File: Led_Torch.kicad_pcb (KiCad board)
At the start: 2 copper layers, 63.8 x 25 mm, 5 parts, among them SW1 SW_DPST_x2

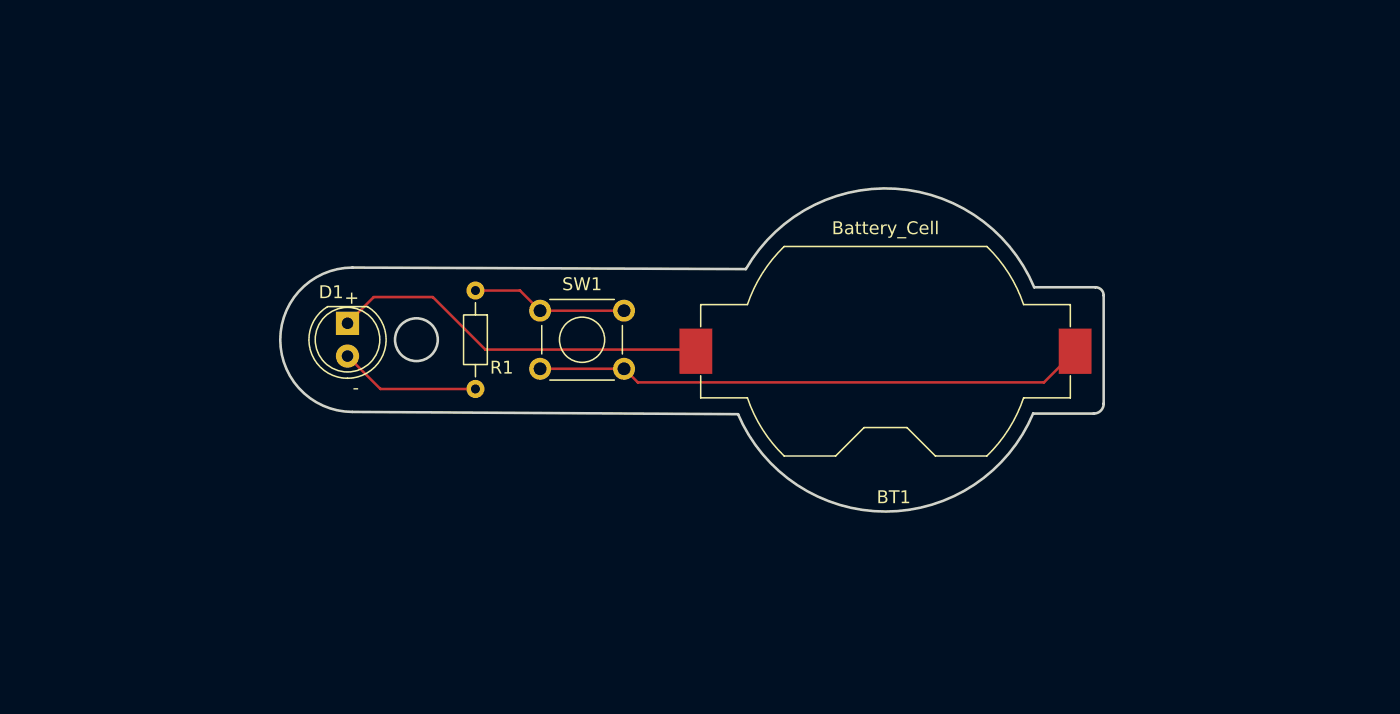
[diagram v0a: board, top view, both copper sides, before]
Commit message: Update: revised schematic/PCB layout, regenerated Gerbers/STEP/views, added copper fill 2D views, fixed company name
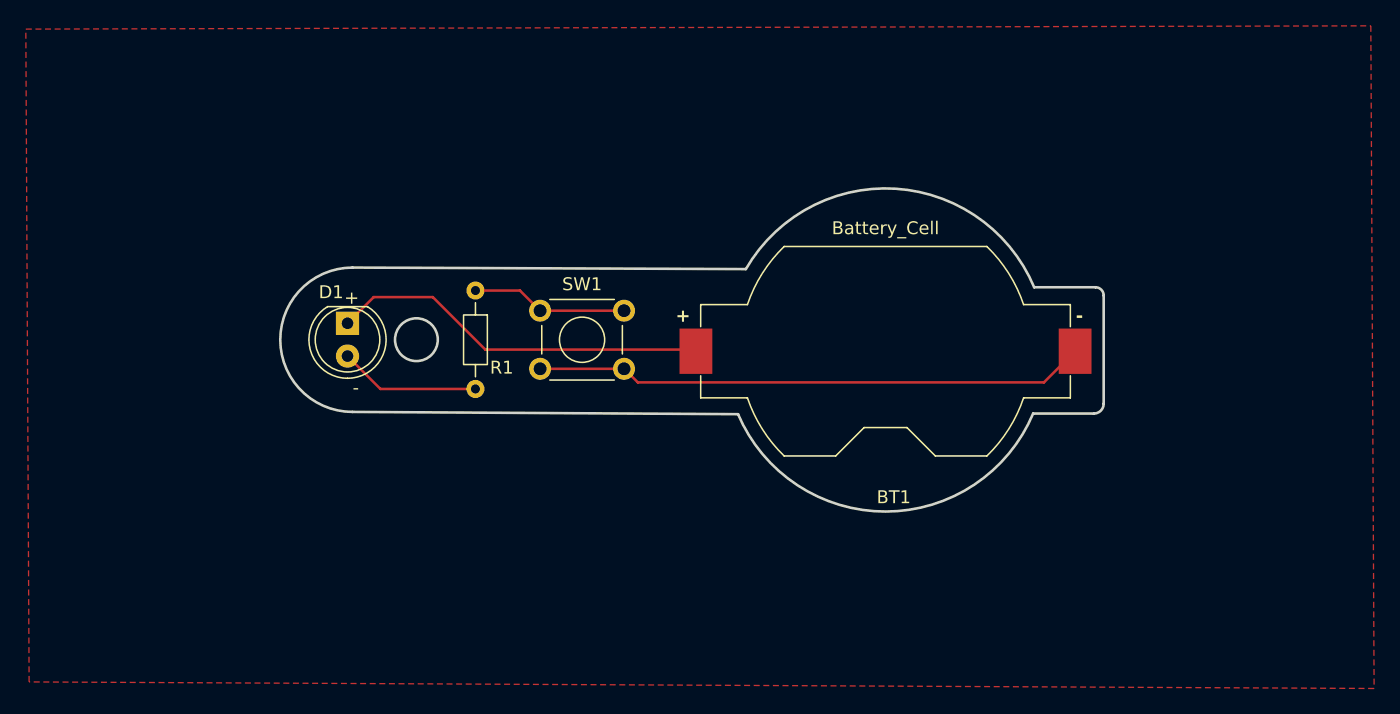
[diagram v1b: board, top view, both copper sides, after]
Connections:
- net /BAT_POS renamed /BAT-
- net /LED_ANODE renamed Net-(D1-A)
- net /LED_CATHODE renamed /BAT+
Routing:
- added copper zone on F.Cu, net /BAT-
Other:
- board text added: "LED TORCH Rev 1.0 Ibrahim Jarallah 2026"
- board text removed: "LED TORCH Rev 1.0 IBrahim Jarallah 2026"
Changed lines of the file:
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@@
 		(rev "1.0")
 		(company "HighTech")
-		(comment 1 "IBrahim Jarallah")
+		(comment 1 "Ibrahim Jarallah")
 	)
 	(layers
@@
 			(drillshape 0)
 			(scaleselection 1)
-			(outputdirectory "Gerbers/")
+			(outputdirectory "Gerbers+drills/")
 		)
 	)
 	(net 0 "")
-	(net 1 "/BAT_POS")
-	(net 2 "/LED_ANODE")
+	(net 1 "/BAT+")
+	(net 2 "/BAT-")
 	(net 3 "Net-(SW1A-A)")
-	(net 4 "/LED_CATHODE")
+	(net 4 "Net-(D1-A)")
 	(footprint "Button_Switch_THT:SW_TH_Tactile_Omron_B3F-100x"
 		(layer "F.Cu")
@@
 			(layers "*.Cu" "*.Mask")
 			(remove_unused_layers no)
-			(net 1 "/BAT_POS")
+			(net 2 "/BAT-")
 			(pinfunction "B")
 			(pintype "passive")
@@
 			(layers "*.Cu" "*.Mask")
 			(remove_unused_layers no)
-			(net 1 "/BAT_POS")
+			(net 2 "/BAT-")
 			(pinfunction "B")
 			(pintype "passive")
@@
 			(size 2.54 3.51)
 			(layers "F.Cu" "F.Mask" "F.Paste")
-			(net 4 "/LED_CATHODE")
+			(net 1 "/BAT+")
 			(pinfunction "+")
 			(pintype "passive")
@@
 			(size 2.54 3.51)
 			(layers "F.Cu" "F.Mask" "F.Paste")
-			(net 1 "/BAT_POS")
+			(net 2 "/BAT-")
 			(pinfunction "-")
 			(pintype "passive")
@@
 			(layers "*.Cu" "*.Mask")
 			(remove_unused_layers no)
-			(net 4 "/LED_CATHODE")
+			(net 1 "/BAT+")
 			(pinfunction "K")
 			(pintype "passive")
@@
 			(layers "*.Cu" "*.Mask")
 			(remove_unused_layers no)
-			(net 2 "/LED_ANODE")
+			(net 4 "Net-(D1-A)")
 			(pinfunction "A")
 			(pintype "passive")
@@
 			(layers "*.Cu" "*.Mask")
 			(remove_unused_layers no)
-			(net 2 "/LED_ANODE")
+			(net 4 "Net-(D1-A)")
 			(pintype "passive")
 		)
@@
 	)
 	(gr_text "+"
+		(at 155.194 93.218 0)
+		(layer "F.SilkS")
+		(effects
+			(font
+				(size 1 1)
+				(thickness 0.2)
+				(bold yes)
+			)
+			(justify left bottom)
+		)
+	)
+	(gr_text "+"
 		(at 129.54 91.821 0)
 		(layer "F.SilkS")
@@
 		)
 	)
-	(gr_text "LED TORCH\nRev 1.0\nIBrahim Jarallah\n2026"
+	(gr_text "-"
+		(at 186.182 93.218 0)
+		(layer "F.SilkS")
+		(effects
+			(font
+				(size 1 1)
+				(thickness 0.2)
+				(bold yes)
+			)
+			(justify left bottom)
+		)
+	)
+	(gr_text "LED TORCH\nRev 1.0\nIbrahim Jarallah\n2026"
 		(at 178.181 101.6 0)
 		(layer "B.SilkS")
@@
 	)
 	(segment
+		(start 136.398 91.186)
+		(end 140.462 95.25)
+		(width 0.2)
+		(layer "F.Cu")
+		(net 1)
+	)
+	(segment
+		(start 129.794 93.213)
+		(end 131.821 91.186)
+		(width 0.2)
+		(layer "F.Cu")
+		(net 1)
+	)
+	(segment
+		(start 140.462 95.25)
+		(end 156.77 95.25)
+		(width 0.2)
+		(layer "F.Cu")
+		(net 1)
+	)
+	(segment
+		(start 131.821 91.186)
+		(end 136.398 91.186)
+		(width 0.2)
+		(layer "F.Cu")
+		(net 1)
+	)
+	(segment
 		(start 186.13 95.377)
 		(end 186.13 95.25)
 		(width 0.2)
 		(layer "F.Cu")
-		(net 1)
+		(net 2)
 	)
 	(segment
@@
 		(width 0.2)
 		(layer "F.Cu")
-		(net 1)
+		(net 2)
 	)
 	(segment
@@
 		(width 0.2)
 		(layer "F.Cu")
-		(net 1)
+		(net 2)
 	)
 	(segment
@@
 		(width 0.2)
 		(layer "F.Cu")
-		(net 1)
+		(net 2)
 	)
 	(segment
@@
 		(width 0.2)
 		(layer "F.Cu")
-		(net 1)
+		(net 2)
 	)
 	(segment
@@
 		(width 0.2)
 		(layer "F.Cu")
-		(net 1)
+		(net 2)
+	)
+	(segment
+		(start 139.7 90.805)
+		(end 139.827 90.678)
+		(width 0.2)
+		(layer "F.Cu")
+		(net 3)
+	)
+	(segment
+		(start 151.205 92.238)
+		(end 151.205 92.365)
+		(width 0.2)
+		(layer "F.Cu")
+		(net 3)
+	)
+	(segment
+		(start 144.705 92.238)
+		(end 151.205 92.238)
+		(width 0.2)
+		(layer "F.Cu")
+		(net 3)
+	)
+	(segment
+		(start 143.145 90.678)
+		(end 144.705 92.238)
+		(width 0.2)
+		(layer "F.Cu")
+		(net 3)
+	)
+	(segment
+		(start 139.827 90.678)
+		(end 143.145 90.678)
+		(width 0.2)
+		(layer "F.Cu")
+		(net 3)
 	)
 	(segment
@@
 		(width 0.2)
 		(layer "F.Cu")
-		(net 2)
+		(net 4)
 	)
 	(segment
@@
 		(width 0.2)
 		(layer "F.Cu")
-		(net 2)
+		(net 4)
 	)
 	(segment
@@
 		(width 0.2)
 		(layer "F.Cu")
-		(net 2)
+		(net 4)
 	)
 	(segment
@@
 		(width 0.2)
 		(layer "F.Cu")
+		(net 4)
+	)
+	(zone
 		(net 2)
-	)
-	(segment
-		(start 139.7 90.805)
-		(end 139.827 90.678)
-		(width 0.2)
-		(layer "F.Cu")
-		(net 3)
-	)
-	(segment
-		(start 151.205 92.238)
-		(end 151.205 92.365)
-		(width 0.2)
-		(layer "F.Cu")
-		(net 3)
-	)
-	(segment
-		(start 144.705 92.238)
-		(end 151.205 92.238)
-		(width 0.2)
-		(layer "F.Cu")
-		(net 3)
-	)
-	(segment
-		(start 143.145 90.678)
-		(end 144.705 92.238)
-		(width 0.2)
-		(layer "F.Cu")
-		(net 3)
-	)
-	(segment
-		(start 139.827 90.678)
-		(end 143.145 90.678)
-		(width 0.2)
-		(layer "F.Cu")
-		(net 3)
-	)
-	(segment
-		(start 136.398 91.186)
-		(end 140.462 95.25)
-		(width 0.2)
-		(layer "F.Cu")
-		(net 4)
-	)
-	(segment
-		(start 129.794 93.213)
-		(end 131.821 91.186)
-		(width 0.2)
-		(layer "F.Cu")
-		(net 4)
-	)
-	(segment
-		(start 140.462 95.25)
-		(end 156.77 95.25)
-		(width 0.2)
-		(layer "F.Cu")
-		(net 4)
-	)
-	(segment
-		(start 131.821 91.186)
-		(end 136.398 91.186)
-		(width 0.2)
-		(layer "F.Cu")
-		(net 4)
+		(net_name "/BAT-")
+		(layer "F.Cu")
+		(hatch edge 0.5)
+		(connect_pads
+			(clearance 0.5)
+		)
+		(min_thickness 0.25)
+		(filled_areas_thickness no)
+		(fill yes
+			(thermal_gap 0.5)
+			(thermal_bridge_width 0.5)
+			(island_removal_mode 1)
+			(island_area_min 10)
+		)
+		(polygon
+			(pts
+				(xy 104.886433 70.436097) (xy 209.026433 70.182097) (xy 209.280433 121.490097) (xy 105.140433 120.982097)
+			)
+		)
 	)
 	(embedded_fonts no)
